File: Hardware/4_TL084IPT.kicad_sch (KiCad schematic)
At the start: 34 parts

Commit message: after merge dev
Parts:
- gave numbers to parts that had none: 30

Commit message: add R0603 footprint
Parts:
- C20: footprint (none) -> IVS_FOOTPRINTS:C0603
- R74, R75, R76, R77, R78, R79, R80, R81, R82, R83, R84, R85, R86, R87, R88, R89: footprint (none) -> IVS_FOOTPRINTS:R0603
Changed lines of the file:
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@@
       (effects (font (size 1.27 1.27)) (justify left))
     )
-    (property "Footprint" "" (id 2) (at 75.692 93.98 90)
+    (property "Footprint" "IVS_FOOTPRINTS:R0603" (id 2) (at 75.692 93.98 90)
       (effects (font (size 1.27 1.27)) hide)
     )
@@
       (effects (font (size 1.27 1.27)) (justify left))
     )
-    (property "Footprint" "" (id 2) (at 134.112 128.27 90)
+    (property "Footprint" "IVS_FOOTPRINTS:R0603" (id 2) (at 134.112 128.27 90)
       (effects (font (size 1.27 1.27)) hide)
     )
@@
       (effects (font (size 1.27 1.27)) (justify left))
     )
-    (property "Footprint" "" (id 2) (at 134.112 85.09 90)
+    (property "Footprint" "IVS_FOOTPRINTS:R0603" (id 2) (at 134.112 85.09 90)
       (effects (font (size 1.27 1.27)) hide)
     )
@@
       (effects (font (size 1.27 1.27)) (justify left))
     )
-    (property "Footprint" "" (id 2) (at 103.8352 35.56 0)
+    (property "Footprint" "IVS_FOOTPRINTS:C0603" (id 2) (at 103.8352 35.56 0)
       (effects (font (size 1.27 1.27)) hide)
     )
@@
       (effects (font (size 1.27 1.27)) (justify left))
     )
-    (property "Footprint" "" (id 2) (at 134.112 39.37 90)
+    (property "Footprint" "IVS_FOOTPRINTS:R0603" (id 2) (at 134.112 39.37 90)
       (effects (font (size 1.27 1.27)) hide)
     )
@@
       (effects (font (size 1.27 1.27)) (justify left))
     )
-    (property "Footprint" "" (id 2) (at 87.122 138.43 90)
+    (property "Footprint" "IVS_FOOTPRINTS:R0603" (id 2) (at 87.122 138.43 90)
       (effects (font (size 1.27 1.27)) hide)
     )
@@
       (effects (font (size 1.27 1.27)) (justify left))
     )
-    (property "Footprint" "" (id 2) (at 87.122 48.26 90)
+    (property "Footprint" "IVS_FOOTPRINTS:R0603" (id 2) (at 87.122 48.26 90)
       (effects (font (size 1.27 1.27)) hide)
     )
@@
       (effects (font (size 1.27 1.27)) (justify left))
     )
-    (property "Footprint" "" (id 2) (at 87.122 93.98 90)
+    (property "Footprint" "IVS_FOOTPRINTS:R0603" (id 2) (at 87.122 93.98 90)
       (effects (font (size 1.27 1.27)) hide)
     )
@@
       (effects (font (size 1.27 1.27)) (justify left))
     )
-    (property "Footprint" "" (id 2) (at 75.692 182.88 90)
+    (property "Footprint" "IVS_FOOTPRINTS:R0603" (id 2) (at 75.692 182.88 90)
       (effects (font (size 1.27 1.27)) hide)
     )
@@
       (effects (font (size 1.27 1.27)) (justify left))
     )
-    (property "Footprint" "" (id 2) (at 75.692 138.43 90)
+    (property "Footprint" "IVS_FOOTPRINTS:R0603" (id 2) (at 75.692 138.43 90)
       (effects (font (size 1.27 1.27)) hide)
     )
@@
       (effects (font (size 1.27 1.27)) (justify left))
     )
-    (property "Footprint" "" (id 2) (at 108.712 100.33 90)
+    (property "Footprint" "IVS_FOOTPRINTS:R0603" (id 2) (at 108.712 100.33 90)
       (effects (font (size 1.27 1.27)) hide)
     )
@@
       (effects (font (size 1.27 1.27)) (justify left))
     )
-    (property "Footprint" "" (id 2) (at 108.712 143.51 90)
+    (property "Footprint" "IVS_FOOTPRINTS:R0603" (id 2) (at 108.712 143.51 90)
       (effects (font (size 1.27 1.27)) hide)
     )
@@
       (effects (font (size 1.27 1.27)) (justify left))
     )
-    (property "Footprint" "" (id 2) (at 134.112 173.99 90)
+    (property "Footprint" "IVS_FOOTPRINTS:R0603" (id 2) (at 134.112 173.99 90)
       (effects (font (size 1.27 1.27)) hide)
     )
@@
       (effects (font (size 1.27 1.27)) (justify left))
     )
-    (property "Footprint" "" (id 2) (at 108.712 54.61 90)
+    (property "Footprint" "IVS_FOOTPRINTS:R0603" (id 2) (at 108.712 54.61 90)
       (effects (font (size 1.27 1.27)) hide)
     )
@@
       (effects (font (size 1.27 1.27)) (justify left))
     )
-    (property "Footprint" "" (id 2) (at 75.692 48.26 90)
+    (property "Footprint" "IVS_FOOTPRINTS:R0603" (id 2) (at 75.692 48.26 90)
       (effects (font (size 1.27 1.27)) hide)
     )
@@
       (effects (font (size 1.27 1.27)) (justify left))
     )
-    (property "Footprint" "" (id 2) (at 87.122 182.88 90)
+    (property "Footprint" "IVS_FOOTPRINTS:R0603" (id 2) (at 87.122 182.88 90)
       (effects (font (size 1.27 1.27)) hide)
     )
@@
       (effects (font (size 1.27 1.27)) (justify left))
     )
-    (property "Footprint" "" (id 2) (at 108.712 189.23 90)
-      (effects (font (size 1.27 1.27)) hide)
-    )
+    (property "Footprint" "IVS_FOOTPRINTS:R0603" (id 2) (at 108.712 189.23 90)
+      (effects (font (size 1.27 1.27)) hide)
+    )

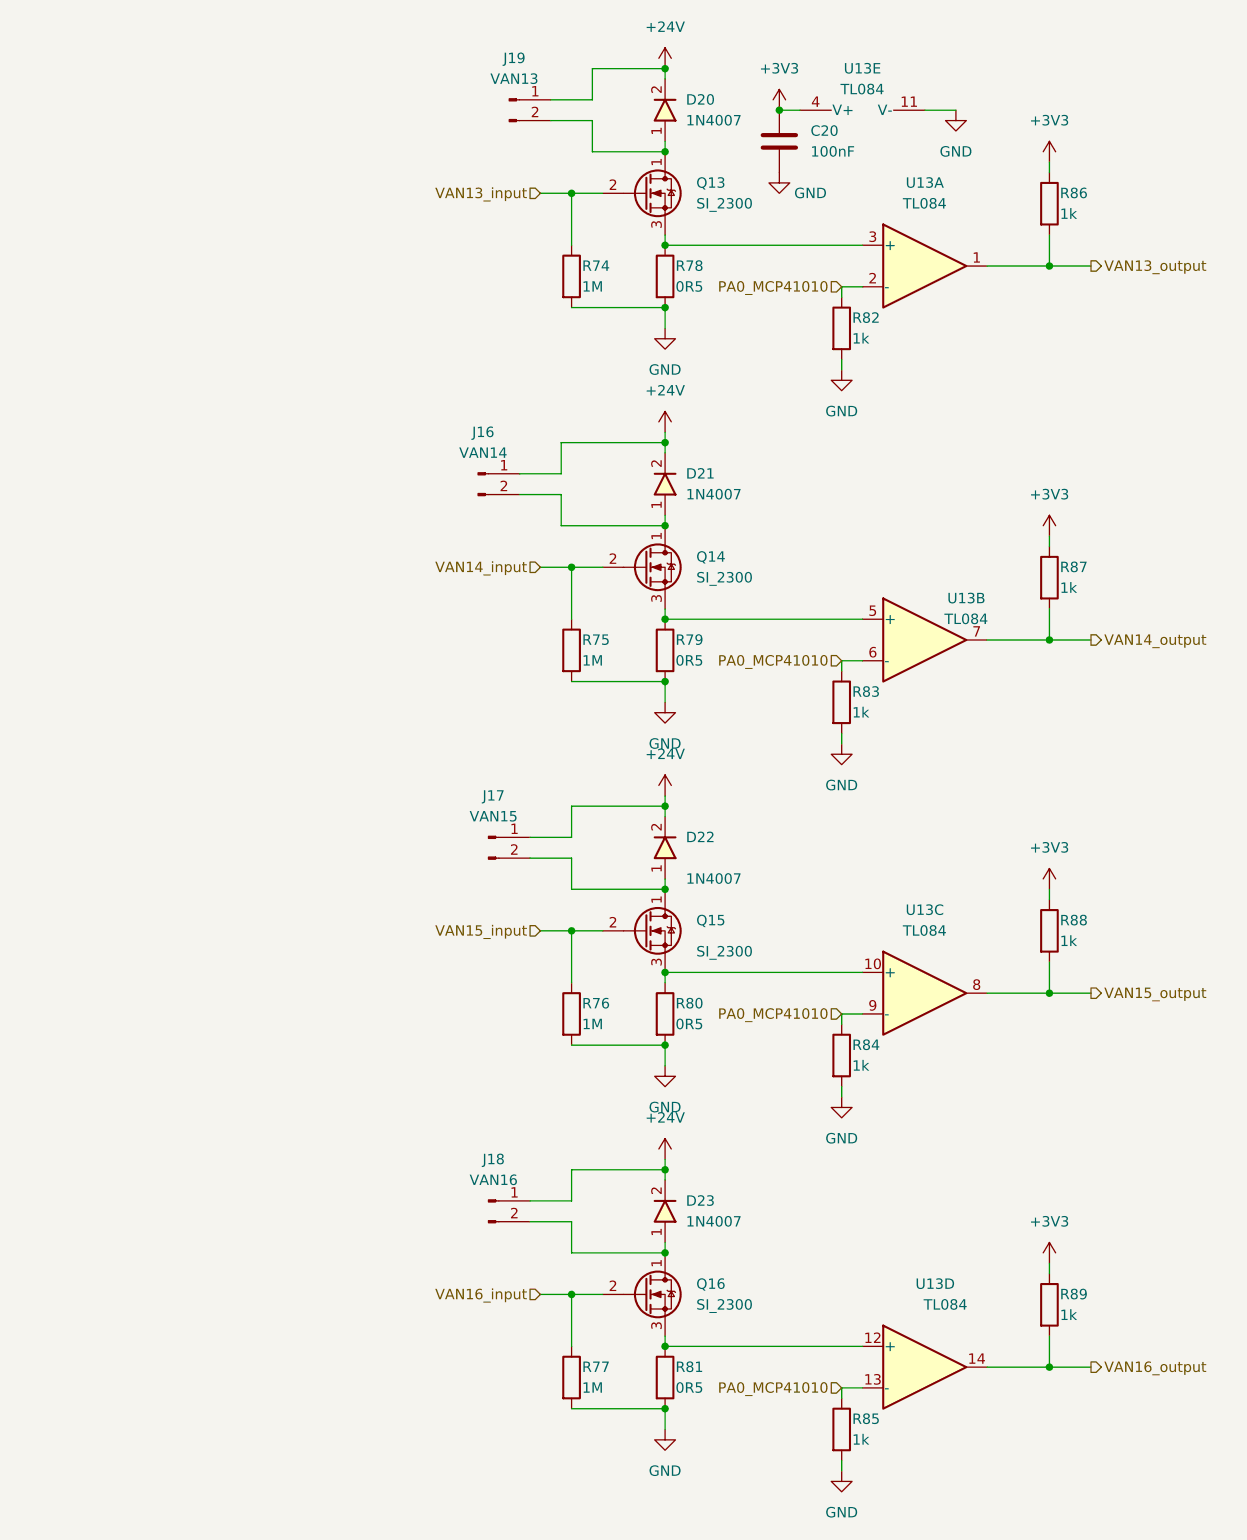
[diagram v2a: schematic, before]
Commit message: fix MCP41010, fix symbol output header
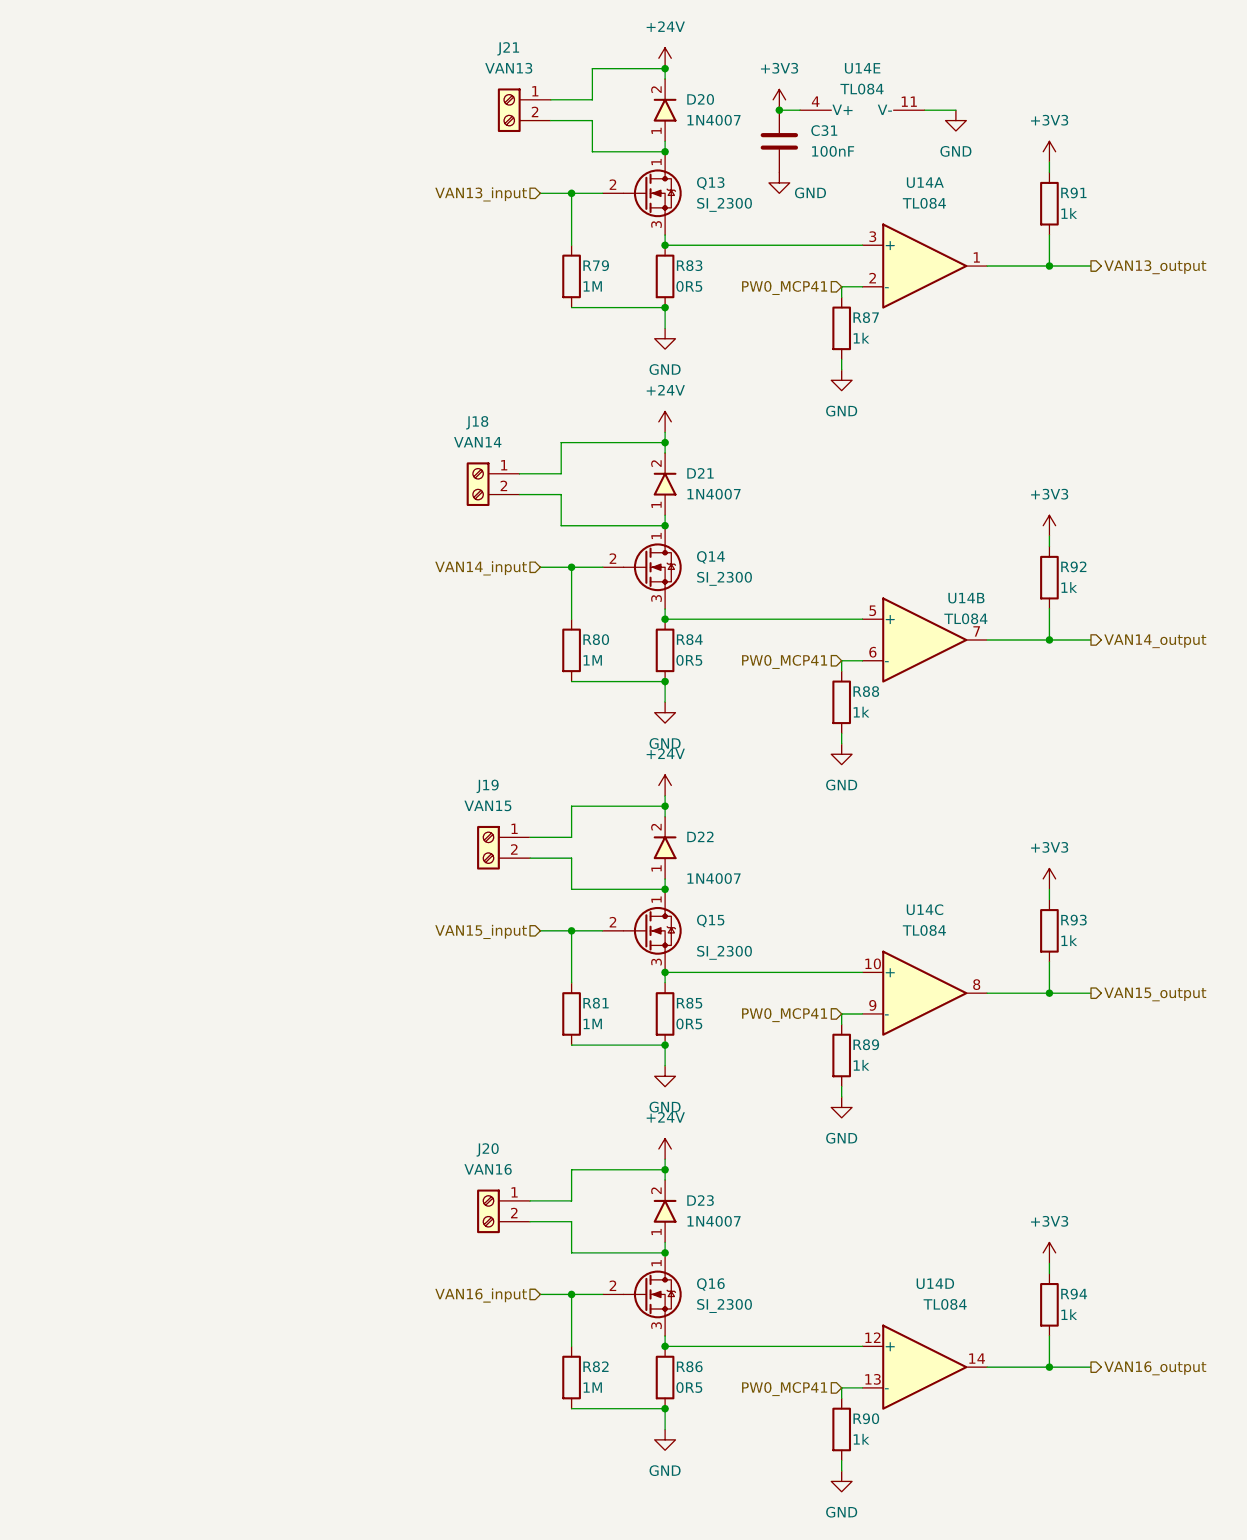
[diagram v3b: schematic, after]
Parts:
- J18: renamed from J16; symbol Connector:Conn_01x02_Male -> Connector:Screw_Terminal_01x02
- J19: renamed from J17; symbol Connector:Conn_01x02_Male -> Connector:Screw_Terminal_01x02
- J20: renamed from J18; symbol Connector:Conn_01x02_Male -> Connector:Screw_Terminal_01x02
- J21: renamed from J19; symbol Connector:Conn_01x02_Male -> Connector:Screw_Terminal_01x02
- R83: renamed from R78; footprint IVS_FOOTPRINTS:R0603 -> Resistor_SMD:R_0805_2012Metric
- R84: renamed from R79; footprint IVS_FOOTPRINTS:R0603 -> Resistor_SMD:R_0805_2012Metric
- R85: renamed from R80; footprint IVS_FOOTPRINTS:R0603 -> Resistor_SMD:R_0805_2012Metric
- R86: renamed from R81; footprint IVS_FOOTPRINTS:R0603 -> Resistor_SMD:R_0805_2012Metric
- renumbered C20 to C31, R74 to R79, R75 to R80, R76 to R81, R77 to R82, R82 to R87, R83 to R88, R84 to R89, R85 to R90, R86 to R91, R87 to R92, R88 to R93, R89 to R94, U13 to U14
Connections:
- net PA0_MCP41010 renamed PW0_MCP41

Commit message: add footprint
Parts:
- removed J18: VAN14, symbol Connector:Screw_Terminal_01x02
- removed J19: VAN15, symbol Connector:Screw_Terminal_01x02
- removed J20: VAN16, symbol Connector:Screw_Terminal_01x02
- removed J21: VAN13, symbol Connector:Screw_Terminal_01x02
- added J?: Screw_Terminal_01x08, IVS_FOOTPRINTS:HT-3.96mm, symbol Connector:Screw_Terminal_01x08
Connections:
- net +24V: now also J?.1 (Pin_1), J?.3 (Pin_3), J?.5 (Pin_5), J?.7 (Pin_7)
- net VAN16-: now reaches D23.1, Q16.1 (D)
- net VAN16-: now also J?.8 (Pin_8)
- net VAN13-: now reaches D20.1, Q13.1 (D)
- net VAN13-: now also J?.2 (Pin_2)
- net VAN14-: now reaches D21.1, Q14.1 (D)
- net VAN14-: now also J?.4 (Pin_4)
- net VAN15-: now reaches D22.1, Q15.1 (D)
- net VAN15-: now also J?.6 (Pin_6)
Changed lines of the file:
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@@
     (stroke (width 0) (type default) (color 0 0 0 0))
+  )
+  (label "VAN16-" (at 27.305 109.22 0)
+    (effects (font (size 1.27 1.27)) (justify left bottom))
+  )
+  (label "VAN16-" (at 72.39 163.83 0)
+    (effects (font (size 1.27 1.27)) (justify left bottom))
+  )
+  (label "VAN14+" (at 71.12 72.39 0)
+    (effects (font (size 1.27 1.27)) (justify left bottom))
+  )
+  (label "VAN14+" (at 27.305 96.52 0)
+    (effects (font (size 1.27 1.27)) (justify left bottom))
+  )
+  (label "VAN14-" (at 71.12 74.93 0)
+    (effects (font (size 1.27 1.27)) (justify left bottom))
+  )
+  (label "VAN13+" (at 74.93 26.67 0)
+    (effects (font (size 1.27 1.27)) (justify left bottom))
+  )
+  (label "VAN13-" (at 27.305 93.98 0)
+    (effects (font (size 1.27 1.27)) (justify left bottom))
+  )
+  (label "VAN15-" (at 27.305 104.14 0)
+    (effects (font (size 1.27 1.27)) (justify left bottom))
+  )
+  (label "VAN15+" (at 72.39 116.84 0)
+    (effects (font (size 1.27 1.27)) (justify left bottom))
+  )
+  (label "VAN13+" (at 27.305 91.44 0)
+    (effects (font (size 1.27 1.27)) (justify left bottom))
+  )
+  (label "VAN16+" (at 27.305 106.68 0)
+    (effects (font (size 1.27 1.27)) (justify left bottom))
+  )
+  (label "VAN13-" (at 74.93 29.21 0)
+    (effects (font (size 1.27 1.27)) (justify left bottom))
+  )
+  (label "VAN14-" (at 27.305 99.06 0)
+    (effects (font (size 1.27 1.27)) (justify left bottom))
+  )
+  (label "VAN15-" (at 72.39 119.38 0)
+    (effects (font (size 1.27 1.27)) (justify left bottom))
+  )
+  (label "VAN15+" (at 27.305 101.6 0)
+    (effects (font (size 1.27 1.27)) (justify left bottom))
+  )
+  (label "VAN16+" (at 72.39 161.29 0)
+    (effects (font (size 1.27 1.27)) (justify left bottom))
   )
   (hierarchical_label "PW0_MCP41" (shape input) (at 110.49 95.25 180)
@@
     (pin "2")
   )
-  (symbol (lib_id "Connector:Screw_Terminal_01x02") (at 67.31 161.29 0) (mirror y) (unit 1)
-    (in_bom yes) (on_board yes) (fields_autoplaced)
-    (property "Reference" "J20" (id 0) (at 67.31 154.94 0))
-    (property "Value" "VAN16" (id 1) (at 67.31 157.48 0))
-    (property "Footprint" "" (id 2) (at 67.31 161.29 0)
-      (effects (font (size 1.27 1.27)) hide)
-    )
-    (property "Datasheet" "~" (id 3) (at 67.31 161.29 0)
-      (effects (font (size 1.27 1.27)) hide)
-    )
-    (pin "1")
-    (pin "2")
-  )
   (symbol (lib_id "power:GND") (at 88.9 100.33 0) (unit 1)
     (in_bom yes) (on_board yes) (fields_autoplaced)
@@
     (pin "2")
   )
-  (symbol (lib_id "Connector:Screw_Terminal_01x02") (at 66.04 72.39 0) (mirror y) (unit 1)
-    (in_bom yes) (on_board yes) (fields_autoplaced)
-    (property "Reference" "J18" (id 0) (at 66.04 66.04 0))
-    (property "Value" "VAN14" (id 1) (at 66.04 68.58 0))
-    (property "Footprint" "" (id 2) (at 66.04 72.39 0)
-      (effects (font (size 1.27 1.27)) hide)
-    )
-    (property "Datasheet" "~" (id 3) (at 66.04 72.39 0)
-      (effects (font (size 1.27 1.27)) hide)
-    )
-    (pin "1")
-    (pin "2")
-  )
   (symbol (lib_id "power:GND") (at 124.46 27.94 0) (unit 1)
     (in_bom yes) (on_board yes) (fields_autoplaced)
@@
     (pin "2")
     (pin "3")
-  )
-  (symbol (lib_id "Connector:Screw_Terminal_01x02") (at 67.31 116.84 0) (mirror y) (unit 1)
-    (in_bom yes) (on_board yes) (fields_autoplaced)
-    (property "Reference" "J19" (id 0) (at 67.31 110.49 0))
-    (property "Value" "VAN15" (id 1) (at 67.31 113.03 0))
-    (property "Footprint" "" (id 2) (at 67.31 116.84 0)
-      (effects (font (size 1.27 1.27)) hide)
-    )
-    (property "Datasheet" "~" (id 3) (at 67.31 116.84 0)
-      (effects (font (size 1.27 1.27)) hide)
-    )
-    (pin "1")
-    (pin "2")
   )
   (symbol (lib_id "power:+3V3") (at 135.89 80.01 0) (unit 1)
@@
     (pin "1")
   )
-  (symbol (lib_id "Connector:Screw_Terminal_01x02") (at 69.85 26.67 0) (mirror y) (unit 1)
-    (in_bom yes) (on_board yes) (fields_autoplaced)
-    (property "Reference" "J21" (id 0) (at 69.85 20.32 0))
-    (property "Value" "VAN13" (id 1) (at 69.85 22.86 0))
-    (property "Footprint" "" (id 2) (at 69.85 26.67 0)
-      (effects (font (size 1.27 1.27)) hide)
-    )
-    (property "Datasheet" "~" (id 3) (at 69.85 26.67 0)
-      (effects (font (size 1.27 1.27)) hide)
-    )
-    (pin "1")
-    (pin "2")
-  )
   (symbol (lib_id "Device:R") (at 88.9 138.43 0) (unit 1)
     (in_bom yes) (on_board yes)
@@
     (pin "2")
   )
+  (symbol (lib_id "Connector:Screw_Terminal_01x08") (at 22.225 99.06 0) (mirror y) (unit 1)
+    (in_bom yes) (on_board yes) (fields_autoplaced)
+    (property "Reference" "J?" (id 0) (at 22.225 85.09 0))
+    (property "Value" "Screw_Terminal_01x08" (id 1) (at 22.225 87.63 0))
+    (property "Footprint" "IVS_FOOTPRINTS:HT-3.96mm" (id 2) (at 22.225 99.06 0)
+      (effects (font (size 1.27 1.27)) hide)
+    )
+    (property "Datasheet" "~" (id 3) (at 22.225 99.06 0)
+      (effects (font (size 1.27 1.27)) hide)
+    )
+    (pin "1")
+    (pin "2")
+    (pin "3")
+    (pin "4")
+    (pin "5")
+    (pin "6")
+    (pin "7")
+    (pin "8")
+  )
   (symbol (lib_id "IVS_SYMBOL_DIR:D_Diode") (at 88.9 26.67 270) (unit 1)
